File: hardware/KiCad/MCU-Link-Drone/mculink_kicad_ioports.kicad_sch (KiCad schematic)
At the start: 12 parts, among them J2 Conn_02x03_Odd_Even, J3 Jumper_2_Open, J4 Jumper_2_Open, J5 Jumper_2_Open, J8 Conn_01x04_Male, SW1 KMR221GLFS, U1 LPC55S69JBD64

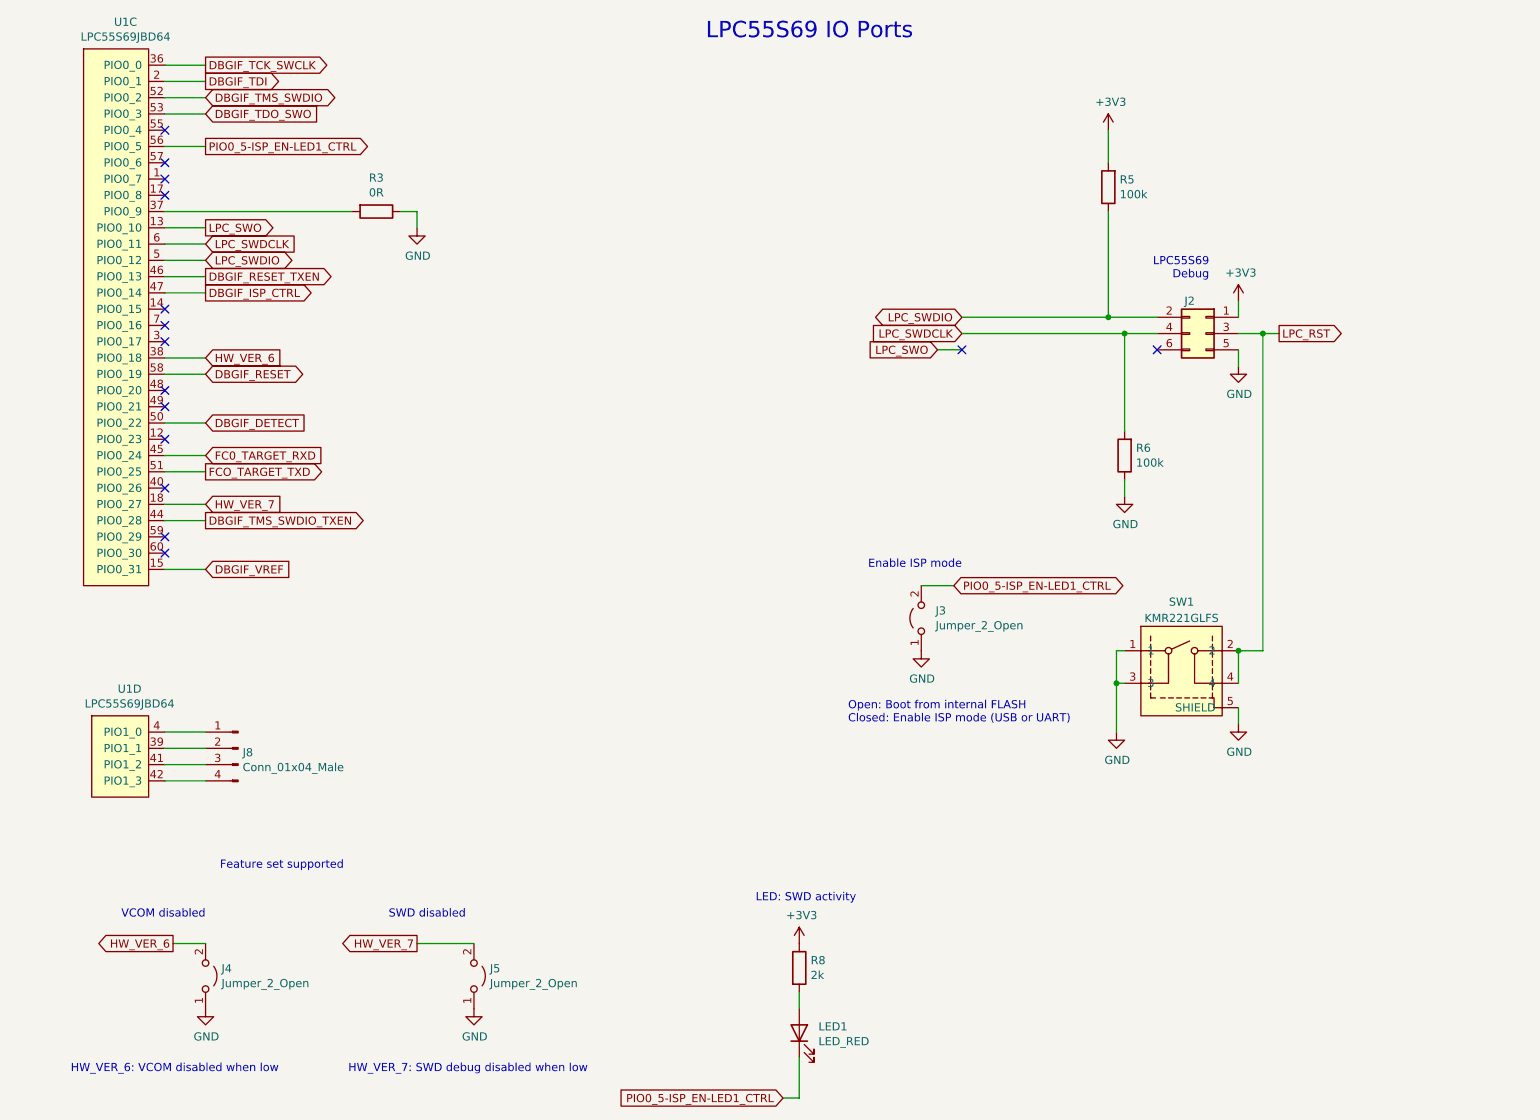
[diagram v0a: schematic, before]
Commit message: updated with drone project files
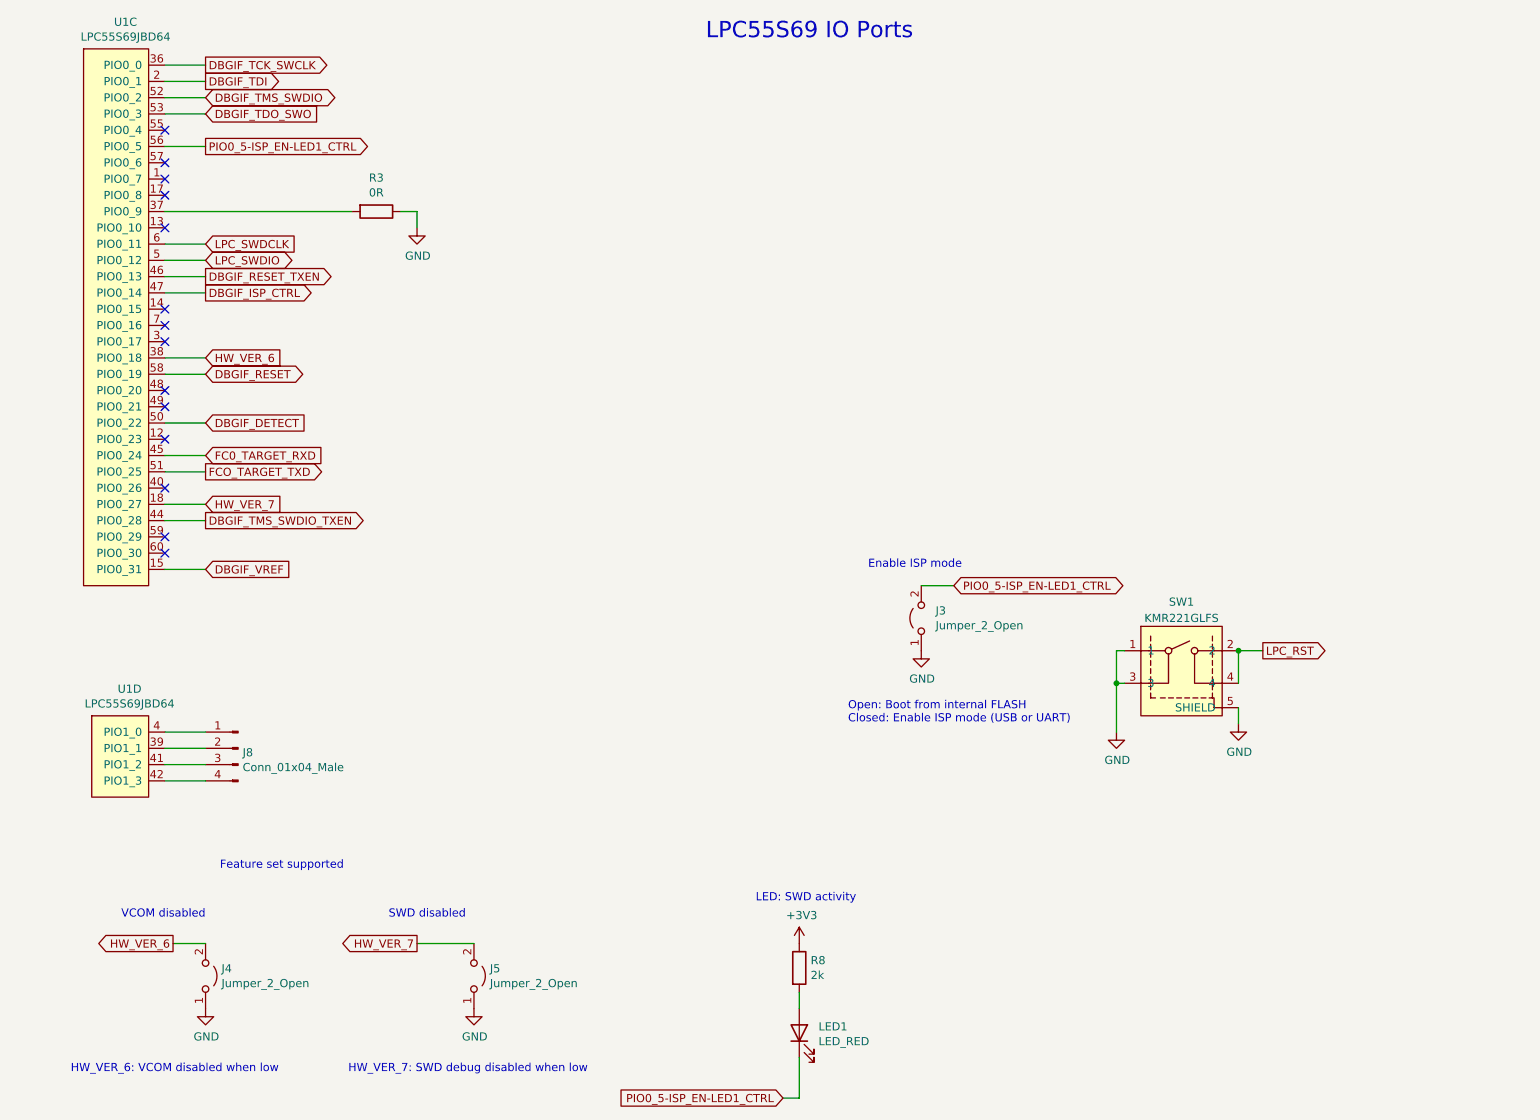
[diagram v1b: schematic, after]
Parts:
- removed J2: Conn_02x03_Odd_Even, mculink_kicad:TAG_TC2030-IDC-NL, symbol Connector_Generic:Conn_02x03_Odd_Even
- removed R5, R6: 100k, Resistor_SMD:R_0603_1608Metric, symbol Device:R
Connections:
- net LPC_SWO: no longer names the net of U1.13 (PIO0_10)
- no-connect marks 15 -> 14
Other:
- note removed: "LPC55S69 Debug"

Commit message: worked on layout
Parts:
- J4, J5: footprint Connector_PinHeader_2.54mm:PinHeader_1x02_P2.54mm_Vertical -> McuOnEclipse:SolderJumper-2_P1.3mm_Open_RoundedPad1.0x1.5mm
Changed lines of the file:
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@@
 			)
 		)
-		(property "Footprint" "Connector_PinHeader_2.54mm:PinHeader_1x02_P2.54mm_Vertical"
+		(property "Footprint" "McuOnEclipse:SolderJumper-2_P1.3mm_Open_RoundedPad1.0x1.5mm"
 			(at 50.8 170.18 0)
 			(effects
@@
 			)
 		)
-		(property "Footprint" "Connector_PinHeader_2.54mm:PinHeader_1x02_P2.54mm_Vertical"
+		(property "Footprint" "McuOnEclipse:SolderJumper-2_P1.3mm_Open_RoundedPad1.0x1.5mm"
 			(at 92.71 170.18 0)
 			(effects

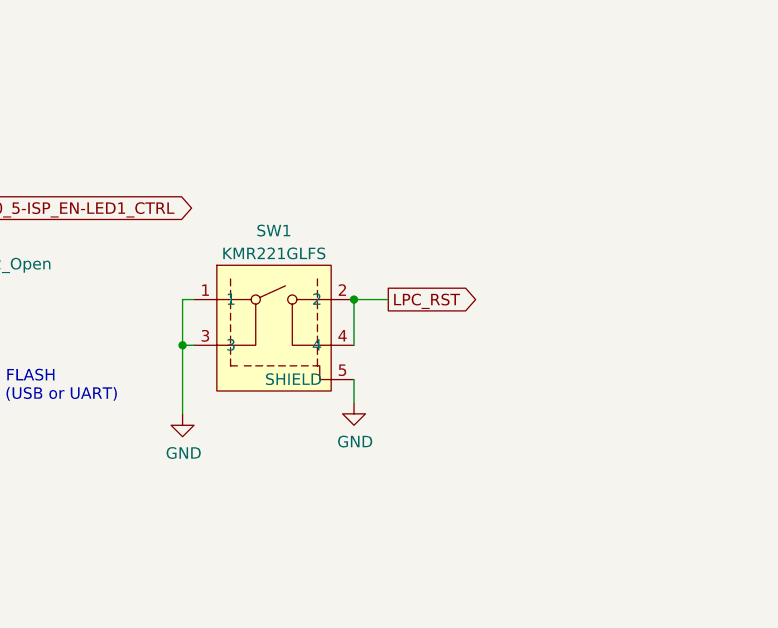
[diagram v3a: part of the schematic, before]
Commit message: added 3D models
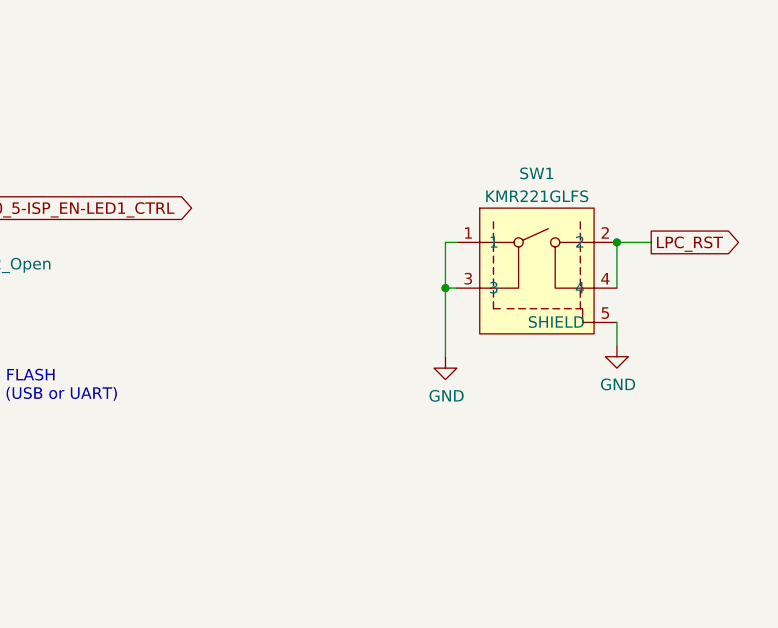
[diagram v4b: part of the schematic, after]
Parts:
- SW1: footprint mculink_kicad:SW_C_K_KMR2 -> McuOnEclipse:SW_C_K_KMR2
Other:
- moved on the sheet: SW1
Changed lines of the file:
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@@
 	)
 	(junction
-		(at 212.09 119.38)
+		(at 241.3 113.03)
 		(diameter 0)
 		(color 0 0 0 0)
 	)
 	(junction
-		(at 193.04 124.46)
+		(at 222.25 118.11)
 		(diameter 0)
 		(color 0 0 0 0)
@@
 	(wire
 		(pts
-			(xy 193.04 124.46) (xy 193.04 132.08)
+			(xy 222.25 118.11) (xy 222.25 125.73)
 		)
 		(stroke
@@
 	(wire
 		(pts
-			(xy 212.09 124.46) (xy 212.09 119.38)
+			(xy 241.3 118.11) (xy 241.3 113.03)
 		)
 		(stroke
@@
 	(wire
 		(pts
-			(xy 194.31 119.38) (xy 193.04 119.38)
+			(xy 223.52 113.03) (xy 222.25 113.03)
 		)
 		(stroke
@@
 	(wire
 		(pts
-			(xy 193.04 119.38) (xy 193.04 124.46)
+			(xy 222.25 113.03) (xy 222.25 118.11)
 		)
 		(stroke
@@
 	(wire
 		(pts
-			(xy 194.31 124.46) (xy 193.04 124.46)
+			(xy 223.52 118.11) (xy 222.25 118.11)
 		)
 		(stroke
@@
 	(wire
 		(pts
-			(xy 212.09 130.81) (xy 212.09 128.27)
+			(xy 241.3 124.46) (xy 241.3 121.92)
 		)
 		(stroke
@@
 	(wire
 		(pts
-			(xy 215.9 119.38) (xy 212.09 119.38)
+			(xy 245.11 113.03) (xy 241.3 113.03)
 		)
 		(stroke
@@
 	(global_label "LPC_RST"
 		(shape output)
-		(at 215.9 119.38 0)
+		(at 245.11 113.03 0)
 		(effects
 			(font
@@
 		)
 		(property "Intersheetrefs" "${INTERSHEET_REFS}"
-			(at 215.9 119.38 0)
+			(at 245.11 113.03 0)
 			(effects
 				(font
@@
 	(symbol
 		(lib_id "mculink_kicad:KMR221GLFS")
-		(at 203.2 124.46 0)
+		(at 232.41 118.11 0)
 		(unit 1)
 		(exclude_from_sim no)
@@
 		(dnp no)
 		(property "Reference" "SW1"
-			(at 203.2 111.76 0)
+			(at 232.41 105.41 0)
 			(effects
 				(font
@@
 		)
 		(property "Value" "KMR221GLFS"
-			(at 203.2 114.3 0)
-			(effects
-				(font
-					(size 1.27 1.27)
-				)
-			)
-		)
-		(property "Footprint" "mculink_kicad:SW_C_K_KMR2"
-			(at 198.12 133.35 0)
+			(at 232.41 107.95 0)
+			(effects
+				(font
+					(size 1.27 1.27)
+				)
+			)
+		)
+		(property "Footprint" "McuOnEclipse:SW_C_K_KMR2"
+			(at 227.33 127 0)
 			(effects
 				(font
@@
 		)
 		(property "Datasheet" ""
-			(at 198.12 133.35 0)
+			(at 227.33 127 0)
 			(effects
 				(font
@@
 		)
 		(property "Description" ""
-			(at 203.2 124.46 0)
+			(at 232.41 118.11 0)
 			(effects
 				(font
@@
 	(symbol
 		(lib_id "power:GND")
-		(at 193.04 132.08 0)
+		(at 222.25 125.73 0)
 		(unit 1)
 		(exclude_from_sim no)
@@
 		(dnp no)
 		(property "Reference" "#PWR040"
-			(at 193.04 138.43 0)
+			(at 222.25 132.08 0)
 			(effects
 				(font
@@
 		)
 		(property "Value" "GND"
-			(at 193.167 136.4742 0)
+			(at 222.377 130.1242 0)
 			(effects
 				(font
@@
 		)
 		(property "Footprint" ""
-			(at 193.04 132.08 0)
+			(at 222.25 125.73 0)
 			(effects
 				(font
@@
 		)
 		(property "Datasheet" ""
-			(at 193.04 132.08 0)
+			(at 222.25 125.73 0)
 			(effects
 				(font
@@
 		)
 		(property "Description" "Power symbol creates a global label with name \"GND\" , ground"
-			(at 193.04 132.08 0)
+			(at 222.25 125.73 0)
 			(effects
 				(font
@@
 	(symbol
 		(lib_id "power:GND")
-		(at 212.09 130.81 0)
+		(at 241.3 124.46 0)
 		(unit 1)
 		(exclude_from_sim no)
@@
 		(dnp no)
 		(property "Reference" "#PWR041"
-			(at 212.09 137.16 0)
+			(at 241.3 130.81 0)
 			(effects
 				(font
@@
 		)
 		(property "Value" "GND"
-			(at 212.217 135.2042 0)
+			(at 241.427 128.8542 0)
 			(effects
 				(font
@@
 		)
 		(property "Footprint" ""
-			(at 212.09 130.81 0)
+			(at 241.3 124.46 0)
 			(effects
 				(font
@@
 		)
 		(property "Datasheet" ""
-			(at 212.09 130.81 0)
+			(at 241.3 124.46 0)
 			(effects
 				(font
@@
 		)
 		(property "Description" "Power symbol creates a global label with name \"GND\" , ground"
-			(at 212.09 130.81 0)
-			(effects
-				(font
+			(at 241.3 124.46 0)
+			(effects
+				(font

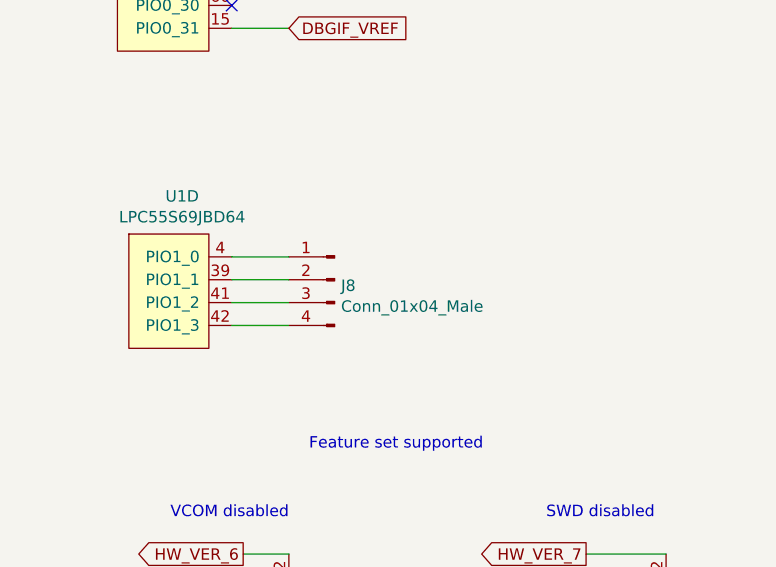
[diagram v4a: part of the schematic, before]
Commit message: fixed warnings
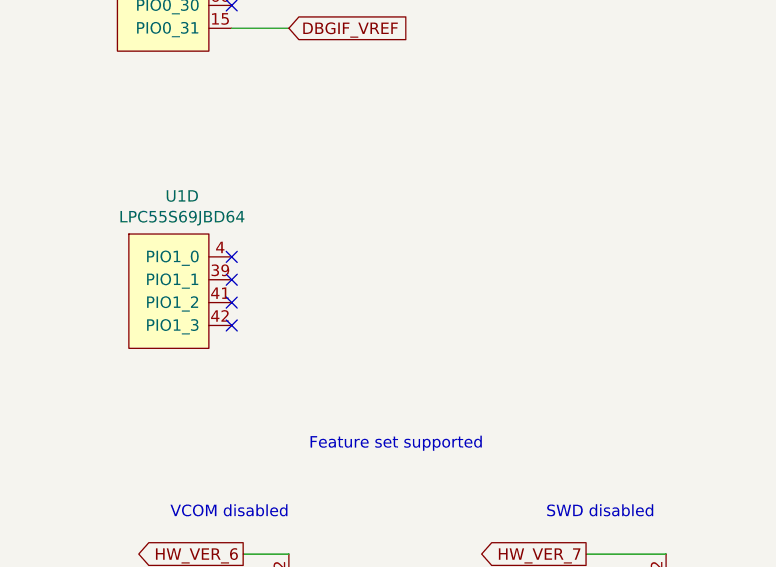
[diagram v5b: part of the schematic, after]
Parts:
- removed J8: Conn_01x04_Male, Connector_PinHeader_1.27mm:PinHeader_1x04_P1.27mm_Vertical, symbol mculink_kicad-rescue:Conn_01x04_Male-Connector
- U1: footprint Package_QFP:LQFP-64-1EP_10x10mm_P0.5mm_EP6.5x6.5mm_ThermalVias -> McuOnEclipse:LQFP-64-1EP_10x10mm_P0.5mm_EP5x5mm
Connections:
- no-connect marks 14 -> 18
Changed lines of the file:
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@@
+	)
+	(no_connect
+		(at 44.45 134.62)
+	)
+	(no_connect
+		(at 44.45 132.08)
 	)
 	(no_connect
@@
 	)
 	(no_connect
+		(at 44.45 137.16)
+	)
+	(no_connect
 		(at 44.45 93.98)
 	)
@@
 	)
 	(no_connect
+		(at 44.45 139.7)
+	)
+	(no_connect
 		(at 44.45 68.58)
 	)
@@
 	(wire
 		(pts
-			(xy 44.45 139.7) (xy 50.8 139.7)
-		)
-		(stroke
-			(width 0)
-			(type default)
-		)
-	)
-	(wire
-		(pts
 			(xy 143.51 172.72) (xy 143.51 175.26)
 		)
@@
 	(wire
 		(pts
-			(xy 44.45 132.08) (xy 50.8 132.08)
-		)
-		(stroke
-			(width 0)
-			(type default)
-		)
-	)
-	(wire
-		(pts
 			(xy 143.51 189.23) (xy 140.97 189.23)
 		)
@@
 	(wire
 		(pts
-			(xy 44.45 134.62) (xy 50.8 134.62)
-		)
-		(stroke
-			(width 0)
-			(type default)
-		)
-	)
-	(wire
-		(pts
 			(xy 223.52 118.11) (xy 222.25 118.11)
 		)
@@
 		(pts
 			(xy 44.45 73.66) (xy 50.8 73.66)
-		)
-		(stroke
-			(width 0)
-			(type default)
-		)
-	)
-	(wire
-		(pts
-			(xy 44.45 137.16) (xy 50.8 137.16)
 		)
 		(stroke
@@
 			)
 		)
-		(property "Footprint" "Package_QFP:LQFP-64-1EP_10x10mm_P0.5mm_EP6.5x6.5mm_ThermalVias"
+		(property "Footprint" "McuOnEclipse:LQFP-64-1EP_10x10mm_P0.5mm_EP5x5mm"
 			(at 33.02 19.05 0)
 			(effects
@@
 			)
 		)
-		(property "Footprint" "Package_QFP:LQFP-64-1EP_10x10mm_P0.5mm_EP6.5x6.5mm_ThermalVias"
+		(property "Footprint" "McuOnEclipse:LQFP-64-1EP_10x10mm_P0.5mm_EP5x5mm"
 			(at 33.02 86.36 0)
 			(effects
@@
 					(unit 1)
 				)
-			)
-		)
-	)
-	(symbol
-		(lib_id "mculink_kicad-rescue:Conn_01x04_Male-Connector")
-		(at 55.88 134.62 0)
-		(mirror y)
-		(unit 1)
-		(exclude_from_sim no)
-		(in_bom yes)
-		(on_board yes)
-		(dnp no)
-		(property "Reference" "J8"
-			(at 56.5912 135.2804 0)
-			(effects
-				(font
-					(size 1.27 1.27)
-				)
-				(justify right)
-			)
-		)
-		(property "Value" "Conn_01x04_Male"
-			(at 56.5912 137.5918 0)
-			(effects
-				(font
-					(size 1.27 1.27)
-				)
-				(justify right)
-			)
-		)
-		(property "Footprint" "Connector_PinHeader_1.27mm:PinHeader_1x04_P1.27mm_Vertical"
-			(at 55.88 134.62 0)
-			(effects
-				(font
-					(size 1.27 1.27)
-				)
-				(hide yes)
-			)
-		)
-		(property "Datasheet" "~"
-			(at 55.88 134.62 0)
-			(effects
-				(font
-					(size 1.27 1.27)
-				)
-				(hide yes)
-			)
-		)
-		(property "Description" ""
-			(at 55.88 134.62 0)
-			(effects
-				(font
-					(size 1.27 1.27)
-				)
-				(hide yes)
-			)
-		)
-		(pin "1"
-		)
-		(pin "2"
-		)
-		(pin "3"
-		)
-		(pin "4"
-		)
-		(instances
-			(project "mculink_drone_kicad"
-				(path "/5d025764-753a-4b80-8d3d-c9a8a22c9527/00000000-0000-0000-0000-0000603cfdf2"
-					(reference "J8")
-					(unit 1)
-				)

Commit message: improved layout
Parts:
- U1: footprint McuOnEclipse:LQFP-64-1EP_10x10mm_P0.5mm_EP5x5mm -> McuOnEclipse:LQFP-64-1EP_10x10mm_P0.5mm_EP3.5x3.5mm
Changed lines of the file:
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@@
 			)
 		)
-		(property "Footprint" "McuOnEclipse:LQFP-64-1EP_10x10mm_P0.5mm_EP5x5mm"
+		(property "Footprint" "McuOnEclipse:LQFP-64-1EP_10x10mm_P0.5mm_EP3.5x3.5mm"
 			(at 33.02 19.05 0)
 			(effects
@@
 			)
 		)
-		(property "Footprint" "McuOnEclipse:LQFP-64-1EP_10x10mm_P0.5mm_EP5x5mm"
+		(property "Footprint" "McuOnEclipse:LQFP-64-1EP_10x10mm_P0.5mm_EP3.5x3.5mm"
 			(at 33.02 86.36 0)
 			(effects

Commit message: optimized layout
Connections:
- net DBGIF_ISP_CTRL: no longer names the net of U1.47 (PIO0_14)
- no-connect marks 18 -> 19
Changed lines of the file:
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@@
+	)
+	(no_connect
+		(at 44.45 63.5)
 	)
 	(no_connect
@@
 		(pts
 			(xy 50.8 60.96) (xy 44.45 60.96)
-		)
-		(stroke
-			(width 0)
-			(type default)
-		)
-	)
-	(wire
-		(pts
-			(xy 44.45 63.5) (xy 50.8 63.5)
 		)
 		(stroke
@@
 			(effects
 				(font
-					(size 1.27 1.27)
-				)
-				(hide yes)
-			)
-		)
-	)
-	(global_label "DBGIF_ISP_CTRL"
-		(shape output)
-		(at 50.8 63.5 0)
-		(effects
-			(font
-				(size 1.27 1.27)
-			)
-			(justify left)
-		)
-		(property "Intersheetrefs" "${INTERSHEET_REFS}"
-			(at 50.8 63.5 0)
-			(effects
-				(font

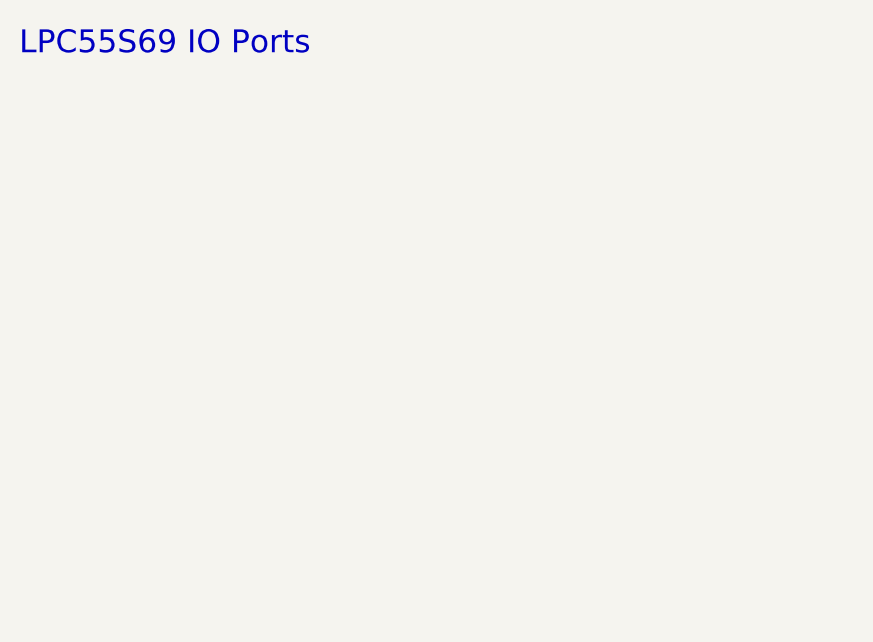
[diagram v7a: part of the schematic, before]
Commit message: updated schematics
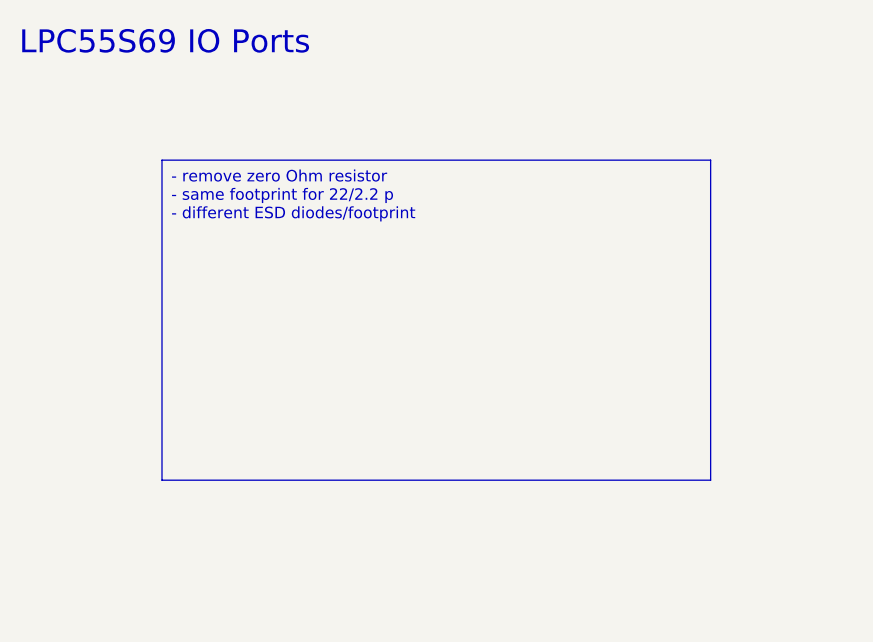
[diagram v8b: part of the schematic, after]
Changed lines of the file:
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@@
+		)
+	)
+	(text_box "- remove zero Ohm resistor\n- same footprint for 22/2.2 p\n- different ESD diodes/footprint"
+		(exclude_from_sim no)
+		(at 144.78 35.56 0)
+		(size 60.96 35.56)
+		(stroke
+			(width 0)
+			(type default)
+		)
+		(fill
+			(type none)
+		)
+		(effects
+			(font
+				(size 1.27 1.27)
+			)
+			(justify left top)
 		)
 	)
